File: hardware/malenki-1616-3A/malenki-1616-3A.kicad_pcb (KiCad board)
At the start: 2 copper layers, 19 x 24.1 mm, 28 parts, among them J1 Conn_01x02_Male, J2 Conn_01x08_Male, J3 Conn_01x02, J5 Conn_01x02_Male, J6 Conn_01x02_Male, J7 Conn_01x02_Male, U1 A7105-MODULE, U2 AIC1734-33GUTR, U3 ATtiny1616-M, U5 DRV8837DSGR, U6 DRV8837DSGR, U7 DRV8837DSGR

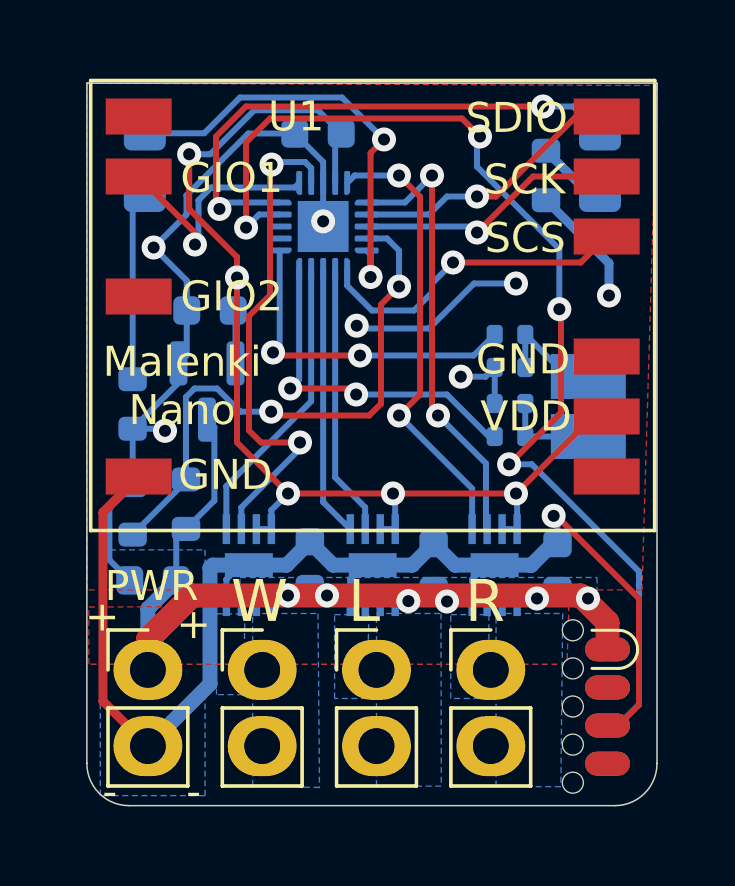
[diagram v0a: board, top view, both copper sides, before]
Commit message: Updated PCB layout to support the additional capacitors and increased trace width where possible for GND to support the higher current.
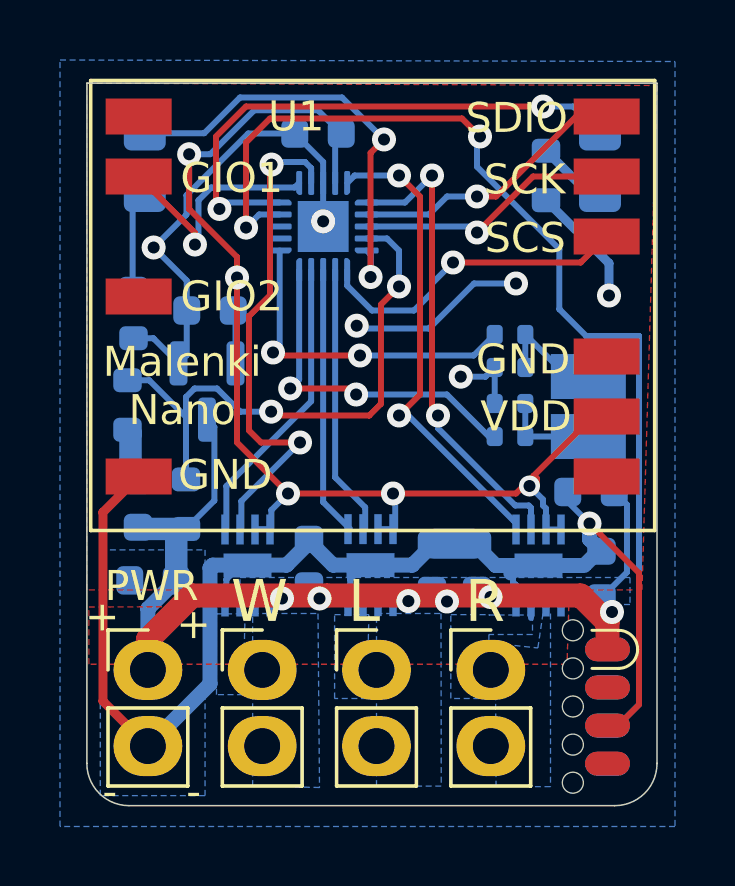
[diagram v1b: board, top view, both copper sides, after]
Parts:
- added C10: 0.1uF 25V X7R, Capacitor_SMD:C_0603_1608Metric, B.Cu at (153.6, 78.1)
- added C8: 0.1uF 25V X7R, Capacitor_SMD:C_0603_1608Metric, B.Cu at (138.1, 75.8)
- added C9: 0.1uF 25V X7R, Capacitor_SMD:C_0603_1608Metric, B.Cu at (149.4, 77.8)
- U5, U6, U7: value DRV8837DSGR -> DRV8212PDSGR
- moved R4 3.50 mm to (137.8, 72.5), turned to -90 degrees
- moved R1 3.02 mm to (137.9, 69.4)
- moved C7 2.74 mm to (153.2, 75.3), turned to 180 degrees
- moved U7 1.46 mm to (151.4, 77.8)
- moved C5 0.09 mm to (143.8, 77.7)
- moved U6 0.07 mm to (145.8, 77.8)
- moved C6 0.06 mm to (147.9, 77.9)
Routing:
- net VBAT: track 27.6 -> 33.3 mm
- net GND: track 81.6 -> 77.7 mm, vias 8 -> 7
- net Net-(D1-Pad1): track 6.32 -> 3.31 mm
- net MOTOR3F: track 15.1 -> 16.0 mm
- net VLOGIC: track 40.4 -> 41.2 mm
- net UPDI: track 36.9 -> 36.1 mm, vias 4 -> 2
- net MOTOR3R: track 15.2 -> 16.0 mm
- net Net-(J7-Pad1): track 0.00 -> 0.55 mm

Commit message: Added vias to motor driver thermal pads to sink heat into front layer copper.
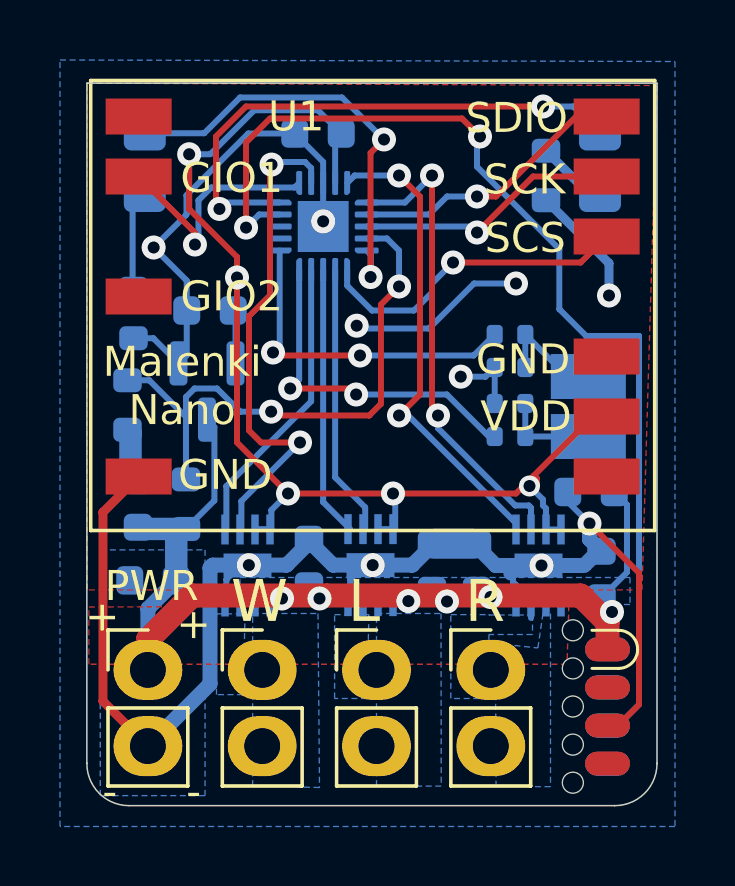
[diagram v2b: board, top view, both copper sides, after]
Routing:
- net GND: vias 7 -> 10
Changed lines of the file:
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@@
   (via (at 138.6215 67.2) (size 0.8) (drill 0.4) (layers "F.Cu" "B.Cu") (net 1))
   (via (at 150.7 68.4) (size 0.8) (drill 0.4) (layers "F.Cu" "B.Cu") (net 1))
+  (via (at 141.7955 77.7875) (size 0.8) (drill 0.4) (layers "F.Cu" "B.Cu") (net 1))
+  (via (at 151.55 77.8) (size 0.8) (drill 0.4) (layers "F.Cu" "B.Cu") (net 1))
   (via (at 153.8 68.8) (size 0.8) (drill 0.4) (layers "F.Cu" "B.Cu") (net 1))
+  (via (at 145.923 77.7875) (size 0.8) (drill 0.4) (layers "F.Cu" "B.Cu") (net 1))
   (via (at 148.858595 71.505493) (size 0.8) (drill 0.4) (layers "F.Cu" "B.Cu") (net 1))
   (segment (start 150.6 78.35) (end 150.7 78.45) (width 0.2) (layer "B.Cu") (net 1))
@@
   (segment (start 141.0455 78.9875) (end 141.0455 78.263478) (width 0.2) (layer "B.Cu") (net 1))
   (segment (start 141.7955 77.7875) (end 143.0525 77.7875) (width 0.5) (layer "B.Cu") (net 1))
+  (segment (start 151.55 77.8) (end 152.975 77.8) (width 0.5) (layer "B.Cu") (net 1))
   (segment (start 149.3 68.4) (end 147.8 69.9) (width 0.2) (layer "B.Cu") (net 1))
   (segment (start 145.483012 69.9) (end 145.389623 69.806611) (width 0.2) (layer "B.Cu") (net 1))
@@
   (segment (start 139.725 70.7875) (end 139.725 69.3) (width 0.2) (layer "B.Cu") (net 1))
   (segment (start 138.43 83.82) (end 140.5 81.75) (width 0.5) (layer "B.Cu") (net 1))
-  (segment (start 151.35 77.8) (end 152.975 77.8) (width 0.5) (layer "B.Cu") (net 1))
+  (segment (start 151.35 77.8) (end 151.55 77.8) (width 0.5) (layer "B.Cu") (net 1))
   (segment (start 153.15 76.4) (end 153.225 76.4) (width 0.2) (layer "B.Cu") (net 1))
   (segment (start 138.43 80.27) (end 139.9 78.8) (width 0.8) (layer "F.Cu") (net 2))
